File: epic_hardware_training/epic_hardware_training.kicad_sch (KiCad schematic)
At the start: 0 parts

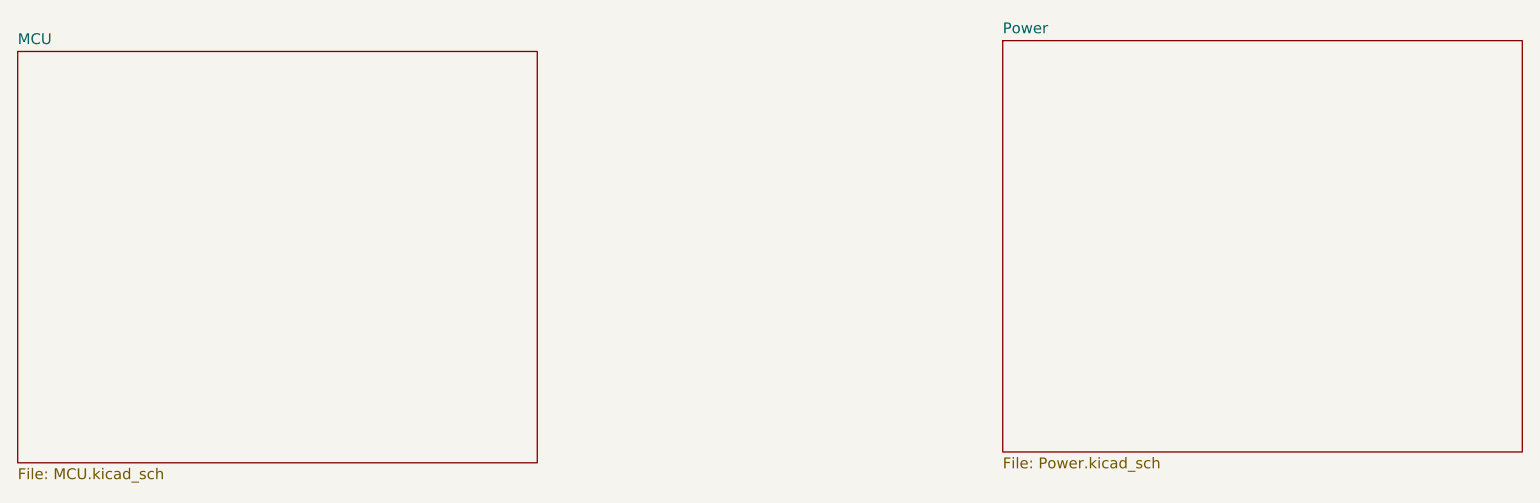
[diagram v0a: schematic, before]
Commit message: complete schematic
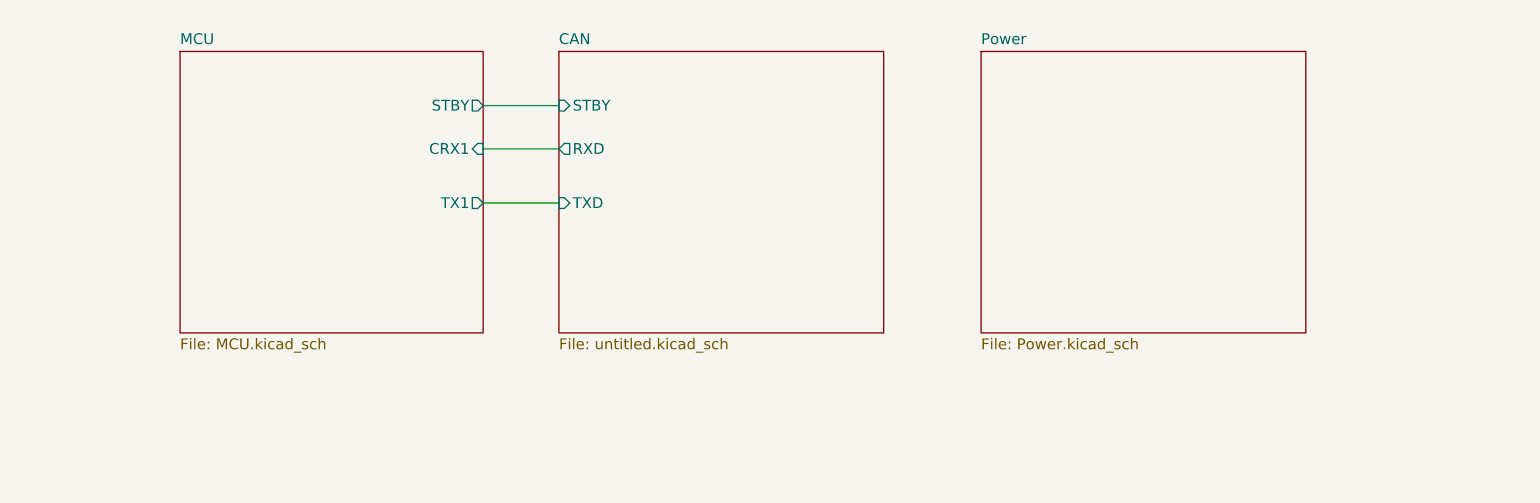
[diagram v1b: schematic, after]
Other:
- added sheet CAN (untitled.kicad_sch)
- sheet MCU ports: added CRX1, STBY, TX1; removed none
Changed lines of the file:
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@@
 	(generator_version "9.0")
 	(paper "A4")
+	(wire
+		(pts
+			(xy 110.49 91.44) (xy 119.38 91.44)
+		)
+		(stroke
+			(width 0)
+			(type default)
+		)
+	)
+	(wire
+		(pts
+			(xy 110.49 97.79) (xy 119.38 97.79)
+		)
+		(stroke
+			(width 0)
+			(type default)
+		)
+	)
+	(wire
+		(pts
+			(xy 110.49 86.36) (xy 119.38 86.36)
+		)
+		(stroke
+			(width 0)
+			(type default)
+		)
+	)
 	(sheet
-		(at 55.88 80.01)
-		(size 60.96 48.26)
+		(at 74.93 80.01)
+		(size 35.56 33.02)
 		(exclude_from_sim no)
 		(in_bom yes)
@@
 		)
 		(property "Sheetname" "MCU"
-			(at 55.88 79.2984 0)
+			(at 74.93 79.2984 0)
 			(effects
 				(font
@@
 		)
 		(property "Sheetfile" "MCU.kicad_sch"
-			(at 55.88 128.8546 0)
+			(at 74.93 113.6146 0)
 			(effects
 				(font
@@
 				)
 				(justify left top)
+			)
+		)
+		(pin "CRX1" input
+			(at 110.49 91.44 0)
+			(effects
+				(font
+					(size 1.27 1.27)
+				)
+				(justify right)
+			)
+		)
+		(pin "TX1" output
+			(at 110.49 97.79 0)
+			(effects
+				(font
+					(size 1.27 1.27)
+				)
+				(justify right)
+			)
+		)
+		(pin "STBY" output
+			(at 110.49 86.36 0)
+			(effects
+				(font
+					(size 1.27 1.27)
+				)
+				(justify right)
 			)
 		)
@@
 	)
 	(sheet
-		(at 171.45 78.74)
-		(size 60.96 48.26)
+		(at 168.91 80.01)
+		(size 38.1 33.02)
 		(exclude_from_sim no)
 		(in_bom yes)
@@
 		)
 		(property "Sheetname" "Power"
-			(at 171.45 78.0284 0)
+			(at 168.91 79.2984 0)
 			(effects
 				(font
@@
 		)
 		(property "Sheetfile" "Power.kicad_sch"
-			(at 171.45 127.5846 0)
+			(at 168.91 113.6146 0)
 			(effects
 				(font
@@
 				)
 			)
+		)
+	)
+	(sheet
+		(at 119.38 80.01)
+		(size 38.1 33.02)
+		(exclude_from_sim no)
+		(in_bom yes)
+		(on_board yes)
+		(dnp no)
+		(fields_autoplaced yes)
+		(stroke
+			(width 0.1524)
+			(type solid)
+		)
+		(fill
+			(color 0 0 0 0.0000)
+		)
+		(property "Sheetname" "CAN"
+			(at 119.38 79.2984 0)
+			(effects
+				(font
+					(size 1.27 1.27)
+				)
+				(justify left bottom)
+			)
+		)
+		(property "Sheetfile" "untitled.kicad_sch"
+			(at 119.38 113.6146 0)
+			(effects
+				(font
+					(size 1.27 1.27)
+				)
+				(justify left top)
+			)
+		)
+		(pin "RXD" output
+			(at 119.38 91.44 180)
+			(effects
+				(font
+					(size 1.27 1.27)
+				)
+				(justify left)
+			)
+		)
+		(pin "STBY" input
+			(at 119.38 86.36 180)
+			(effects
+				(font
+					(size 1.27 1.27)
+				)
+				(justify left)
+			)
+		)
+		(pin "TXD" input
+			(at 119.38 97.79 180)
+			(effects
+				(font
+					(size 1.27 1.27)
+				)
+				(justify left)
+			)
+		)
+		(instances
+			(project "epic_hardware_training"
+				(path "/30ac4f03-b625-4332-b9e2-69de598ec1a0"
+					(page "4")
+				)
+			)
